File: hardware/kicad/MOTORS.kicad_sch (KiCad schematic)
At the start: 40 parts

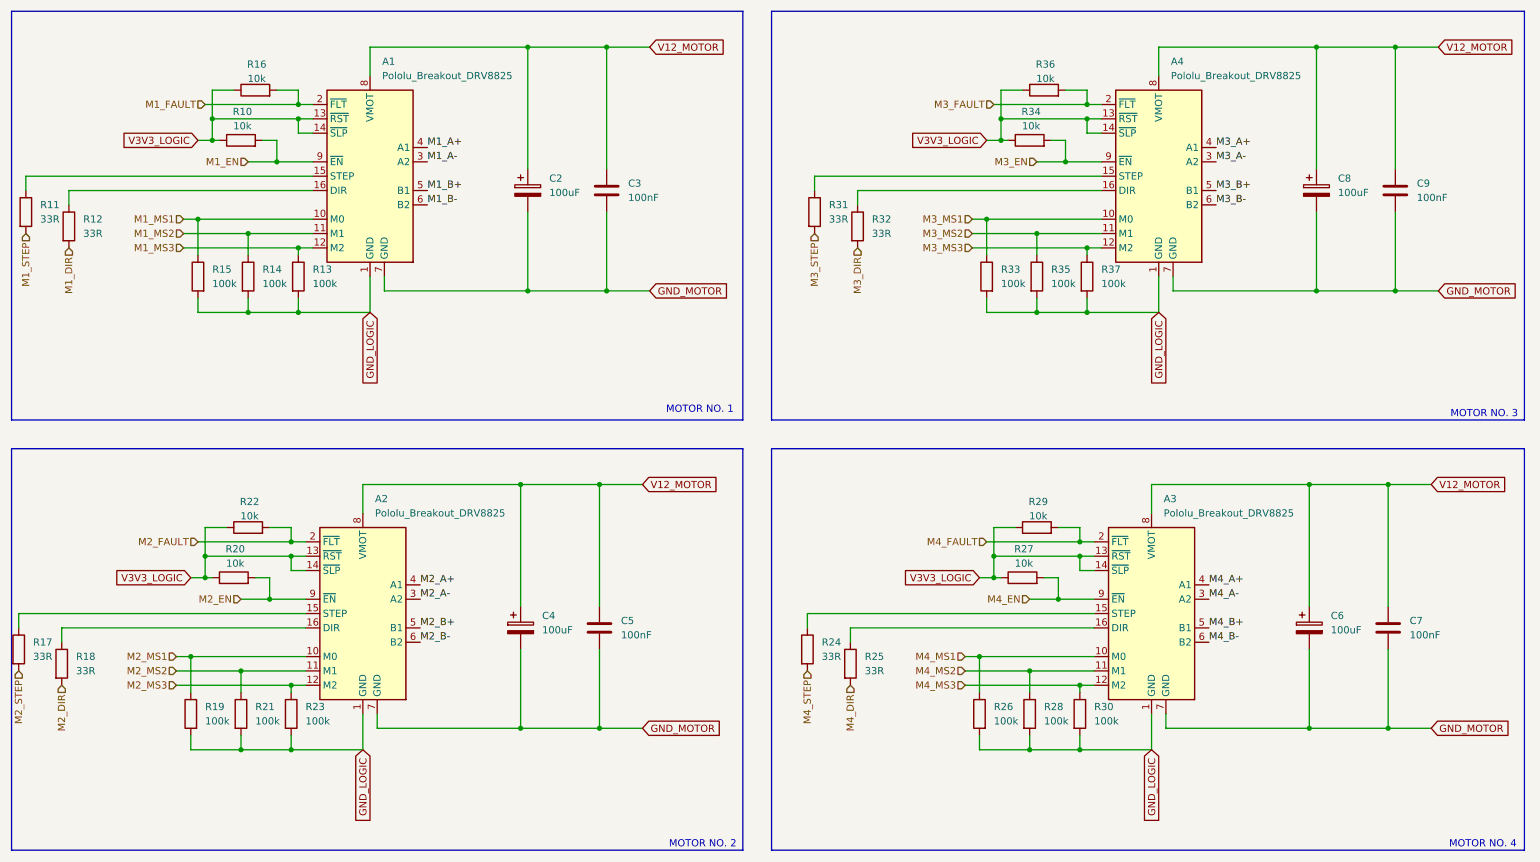
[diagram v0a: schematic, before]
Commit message: fix: error fixing & connection config
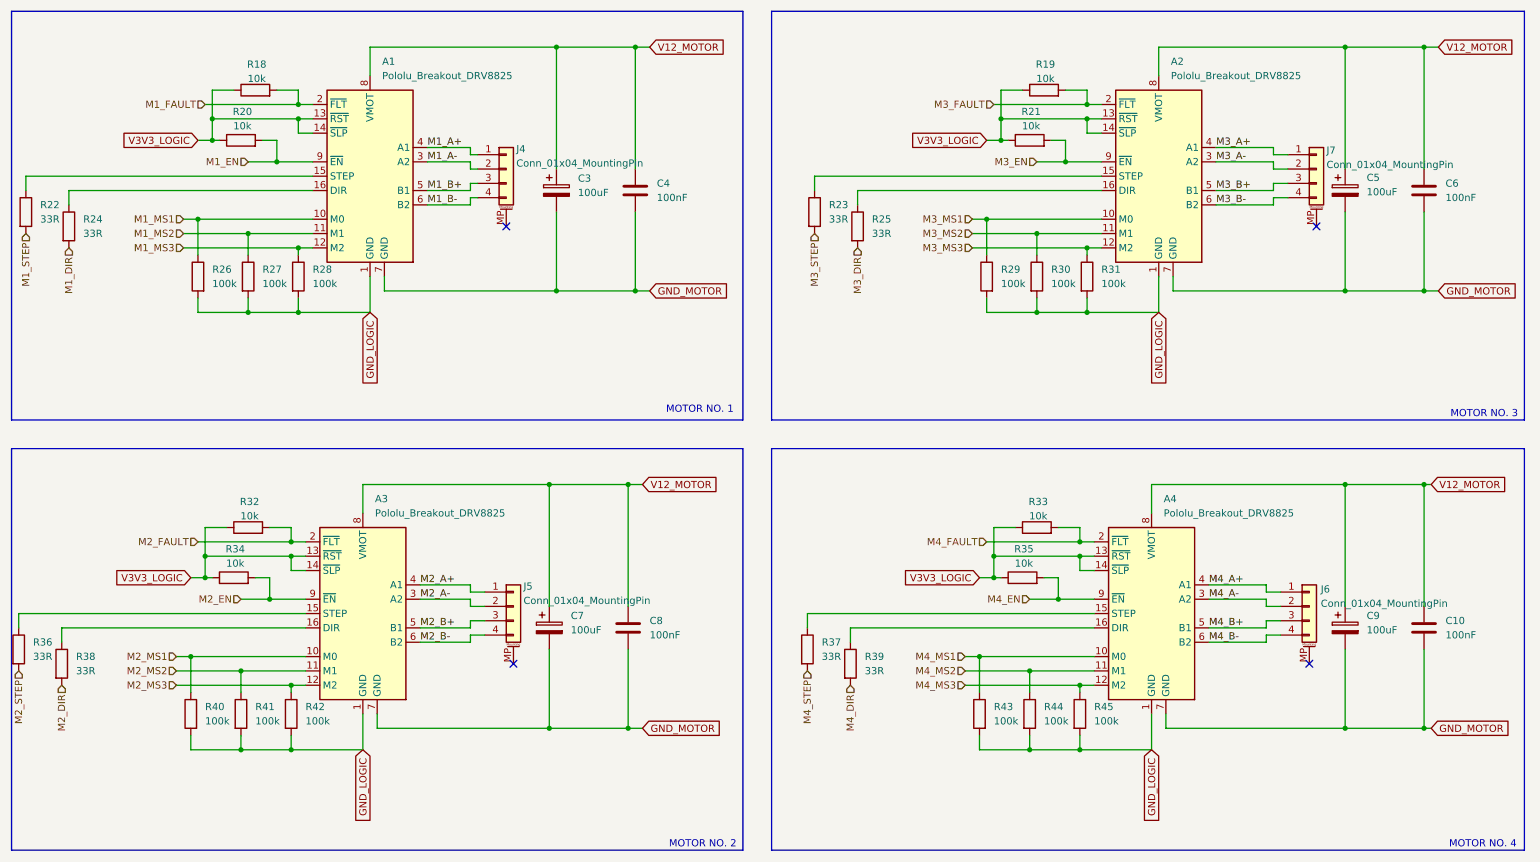
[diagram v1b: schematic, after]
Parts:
- added J4, J5, J6, J7: Conn_01x04_MountingPin, symbol Connector_Generic_MountingPin:Conn_01x04_MountingPin
- renumbered A4 to A2, A2 to A3, A3 to A4, C7 to C10, C2 to C3, C3 to C4, C8 to C5, C9 to C6, C4 to C7, C5 to C8, C6 to C9, R16 to R18, R36 to R19, R10 to R20, R34 to R21, R11 to R22, R31 to R23, R12 to R24, R32 to R25, R15 to R26, R14 to R27, R13 to R28, R33 to R29, R35 to R30, R37 to R31, R22 to R32, R29 to R33, R20 to R34, R27 to R35, R17 to R36, R24 to R37, R18 to R38, R25 to R39, R19 to R40, R21 to R41, R23 to R42, R26 to R43, R28 to R44, R30 to R45
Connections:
- net M1_A+: now also J4.1 (Pin_1)
- net M1_A-: now also J4.2 (Pin_2)
- net M1_B+: now also J4.3 (Pin_3)
- net M1_B-: now also J4.4 (Pin_4)
- net M2_A+: now also J5.1 (Pin_1)
- net M2_A-: now also J5.2 (Pin_2)
- net M2_B+: now also J5.3 (Pin_3)
- net M2_B-: now also J5.4 (Pin_4)
- net M3_A+: now also J7.1 (Pin_1)
- net M3_A-: now also J7.2 (Pin_2)
- net M3_B+: now also J7.3 (Pin_3)
- net M3_B-: now also J7.4 (Pin_4)
- net M4_A+: now also J6.1 (Pin_1)
- net M4_A-: now also J6.2 (Pin_2)
- net M4_B+: now also J6.3 (Pin_3)
- net M4_B-: now also J6.4 (Pin_4)
- no-connect marks 0 -> 4
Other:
- moved on the sheet: C10, C3, C4, C5, C6, C7, C8, C9

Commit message: docs: added end semester report for project
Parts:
- A1, A2, A3, A4: symbol Driver_Motor:Pololu_Breakout_DRV8825 -> TPSM82903:Pololu_Breakout_DRV8825
- C10, C4, C6, C8: symbol Device:C -> TPSM82903:C
- C3, C5, C7, C9: symbol Device:C_Polarized -> TPSM82903:C_Polarized
- J4, J5, J6, J7: symbol Connector_Generic_MountingPin:Conn_01x04_MountingPin -> TPSM82903:Conn_01x04_MountingPin
- R18, R19, R20, R21, R22, R23, R24, R25, R26, R27, R28, R29, R30, R31, R32, R33, R34, R35, R36, R37, R38, R39, R40, R41, R42, R43, R44, R45: symbol Device:R -> TPSM82903:R
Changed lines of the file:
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@@
 	)
 	(symbol
-		(lib_id "Driver_Motor:Pololu_Breakout_DRV8825")
+		(lib_id "TPSM82903:Pololu_Breakout_DRV8825")
 		(at 217.17 120.65 0)
 		(unit 1)
@@
 	)
 	(symbol
-		(lib_id "Device:R")
+		(lib_id "TPSM82903:R")
 		(at 54.61 116.84 90)
 		(unit 1)
@@
 	)
 	(symbol
-		(lib_id "Connector_Generic_MountingPin:Conn_01x04_MountingPin")
+		(lib_id "TPSM82903:Conn_01x04_MountingPin")
 		(at 104.14 121.92 0)
 		(unit 1)
@@
 	)
 	(symbol
-		(lib_id "Connector_Generic_MountingPin:Conn_01x04_MountingPin")
+		(lib_id "TPSM82903:Conn_01x04_MountingPin")
 		(at 246.38 44.45 0)
 		(unit 1)
@@
 	)
 	(symbol
-		(lib_id "Device:R")
+		(lib_id "TPSM82903:R")
 		(at 195.58 140.97 0)
 		(unit 1)
@@
 	)
 	(symbol
-		(lib_id "Device:R")
+		(lib_id "TPSM82903:R")
 		(at 25.4 54.61 0)
 		(unit 1)
@@
 	)
 	(symbol
-		(lib_id "Device:R")
+		(lib_id "TPSM82903:R")
 		(at 204.47 140.97 0)
 		(unit 1)
@@
 	)
 	(symbol
-		(lib_id "Device:R")
+		(lib_id "TPSM82903:R")
 		(at 66.04 63.5 0)
 		(unit 1)
@@
 	)
 	(symbol
-		(lib_id "Device:C_Polarized")
+		(lib_id "TPSM82903:C_Polarized")
 		(at 111.76 48.26 0)
 		(unit 1)
@@
 	)
 	(symbol
-		(lib_id "Device:R")
+		(lib_id "TPSM82903:R")
 		(at 194.31 116.84 90)
 		(unit 1)
@@
 	)
 	(symbol
-		(lib_id "Device:R")
+		(lib_id "TPSM82903:R")
 		(at 196.85 63.5 0)
 		(unit 1)
@@
 	)
 	(symbol
-		(lib_id "Driver_Motor:Pololu_Breakout_DRV8825")
+		(lib_id "TPSM82903:Pololu_Breakout_DRV8825")
 		(at 218.44 43.18 0)
 		(unit 1)
@@
 	)
 	(symbol
-		(lib_id "Device:C")
+		(lib_id "TPSM82903:C")
 		(at 125.73 48.26 0)
 		(unit 1)
@@
 	)
 	(symbol
-		(lib_id "Device:R")
+		(lib_id "TPSM82903:R")
 		(at 16.51 129.54 0)
 		(unit 1)
@@
 	)
 	(symbol
-		(lib_id "Connector_Generic_MountingPin:Conn_01x04_MountingPin")
+		(lib_id "TPSM82903:Conn_01x04_MountingPin")
 		(at 102.87 44.45 0)
 		(unit 1)
@@
 	)
 	(symbol
-		(lib_id "Device:R")
+		(lib_id "TPSM82903:R")
 		(at 157.48 52.07 0)
 		(unit 1)
@@
 	)
 	(symbol
-		(lib_id "Device:R")
+		(lib_id "TPSM82903:R")
 		(at 46.99 140.97 0)
 		(mirror y)
@@
 	)
 	(symbol
-		(lib_id "Device:R")
+		(lib_id "TPSM82903:R")
 		(at 205.74 63.5 0)
 		(unit 1)
@@
 	)
 	(symbol
-		(lib_id "Device:C")
+		(lib_id "TPSM82903:C")
 		(at 265.43 48.26 0)
 		(unit 1)
@@
 	)
 	(symbol
-		(lib_id "Driver_Motor:Pololu_Breakout_DRV8825")
+		(lib_id "TPSM82903:Pololu_Breakout_DRV8825")
 		(at 77.47 120.65 0)
 		(unit 1)
@@
 	)
 	(symbol
-		(lib_id "Device:R")
+		(lib_id "TPSM82903:R")
 		(at 165.1 54.61 0)
 		(unit 1)
@@
 	)
 	(symbol
-		(lib_id "Device:R")
+		(lib_id "TPSM82903:R")
 		(at 55.88 140.97 0)
 		(unit 1)
@@
 	)
 	(symbol
-		(lib_id "Device:R")
+		(lib_id "TPSM82903:R")
 		(at 17.78 52.07 0)
 		(unit 1)
@@
 	)
 	(symbol
-		(lib_id "Device:R")
+		(lib_id "TPSM82903:R")
 		(at 195.58 39.37 90)
 		(unit 1)
@@
 	)
 	(symbol
-		(lib_id "Device:C")
+		(lib_id "TPSM82903:C")
 		(at 265.43 125.73 0)
 		(unit 1)
@@
 	)
 	(symbol
-		(lib_id "Device:R")
+		(lib_id "TPSM82903:R")
 		(at 48.26 63.5 0)
 		(mirror y)
@@
 	)
 	(symbol
-		(lib_id "Device:R")
+		(lib_id "TPSM82903:R")
 		(at 156.21 129.54 0)
 		(unit 1)
@@
 	)
 	(symbol
-		(lib_id "Device:R")
+		(lib_id "TPSM82903:R")
 		(at 198.12 30.48 90)
 		(unit 1)
@@
 	)
 	(symbol
-		(lib_id "Device:R")
+		(lib_id "TPSM82903:R")
 		(at 58.42 30.48 90)
 		(unit 1)
@@
 	)
 	(symbol
-		(lib_id "Device:R")
+		(lib_id "TPSM82903:R")
 		(at 186.69 140.97 0)
 		(mirror y)
@@
 	)
 	(symbol
-		(lib_id "Device:R")
+		(lib_id "TPSM82903:R")
 		(at 57.15 107.95 90)
 		(unit 1)
@@
 	)
 	(symbol
-		(lib_id "Device:C_Polarized")
+		(lib_id "TPSM82903:C_Polarized")
 		(at 251.46 48.26 0)
 		(unit 1)
@@
 	)
 	(symbol
-		(lib_id "Device:R")
+		(lib_id "TPSM82903:R")
 		(at 163.83 132.08 0)
 		(unit 1)
@@
 	)
 	(symbol
-		(lib_id "Device:C")
+		(lib_id "TPSM82903:C")
 		(at 124.46 125.73 0)
 		(unit 1)
@@
 	)
 	(symbol
-		(lib_id "Device:R")
+		(lib_id "TPSM82903:R")
 		(at 64.77 140.97 0)
 		(unit 1)
@@
 	)
 	(symbol
-		(lib_id "Device:R")
+		(lib_id "TPSM82903:R")
 		(at 57.15 63.5 0)
 		(unit 1)
@@
 	)
 	(symbol
-		(lib_id "Connector_Generic_MountingPin:Conn_01x04_MountingPin")
+		(lib_id "TPSM82903:Conn_01x04_MountingPin")
 		(at 245.11 121.92 0)
 		(unit 1)
@@
 	)
 	(symbol
-		(lib_id "Device:C_Polarized")
+		(lib_id "TPSM82903:C_Polarized")
 		(at 110.49 125.73 0)
 		(unit 1)
@@
 	)
 	(symbol
-		(lib_id "Device:R")
+		(lib_id "TPSM82903:R")
 		(at 187.96 63.5 0)
 		(mirror y)
@@
 	)
 	(symbol
-		(lib_id "Driver_Motor:Pololu_Breakout_DRV8825")
+		(lib_id "TPSM82903:Pololu_Breakout_DRV8825")
 		(at 78.74 43.18 0)
 		(unit 1)
@@
 	)
 	(symbol
-		(lib_id "Device:R")
+		(lib_id "TPSM82903:R")
 		(at 196.85 107.95 90)
 		(unit 1)
@@
 	)
 	(symbol
-		(lib_id "Device:R")
+		(lib_id "TPSM82903:R")
 		(at 24.13 132.08 0)
 		(unit 1)
@@
 	)
 	(symbol
-		(lib_id "Device:C_Polarized")
+		(lib_id "TPSM82903:C_Polarized")
 		(at 251.46 125.73 0)
 		(unit 1)
@@
 	)
 	(symbol
-		(lib_id "Device:R")
+		(lib_id "TPSM82903:R")
 		(at 55.88 39.37 90)
 		(unit 1)
